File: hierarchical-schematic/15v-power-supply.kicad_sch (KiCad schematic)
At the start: 25 parts, among them J901 Terminal Block, J902 Terminal Block, P901 120VAC, SW901 0, T901 XFORMER, U901 LM7815, U902 LM7915

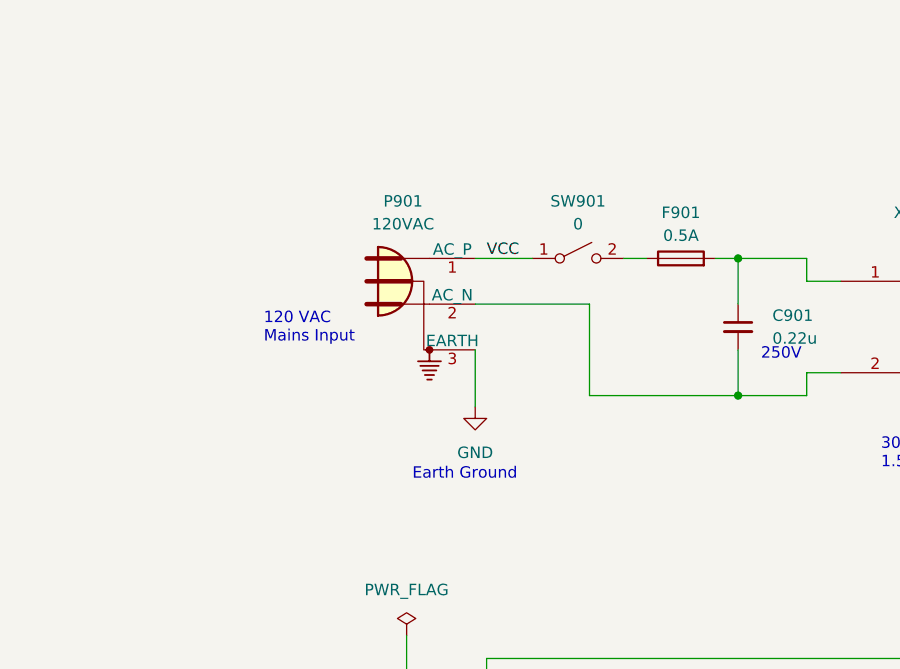
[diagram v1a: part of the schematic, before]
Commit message: updatess to kicad v8
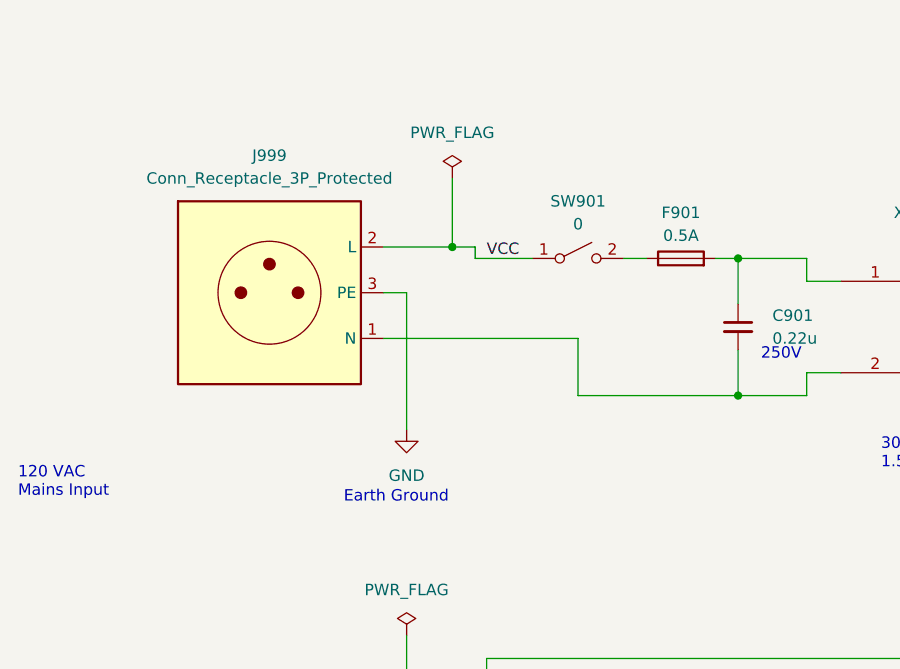
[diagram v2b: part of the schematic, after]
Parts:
- removed P901: 120VAC, symbol Connector:Conn_WallPlug_Earth
- added J999: Conn_Receptacle_3P_Protected, symbol Connector:Conn_Receptacle_3P_Protected
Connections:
- net GND: now also J999.3 (PE)
- net VCC: now also J999.2 (L)
- net at C901.2, T901.2 (AB): now also J999.1 (N)
